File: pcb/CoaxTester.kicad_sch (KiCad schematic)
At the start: 14 parts

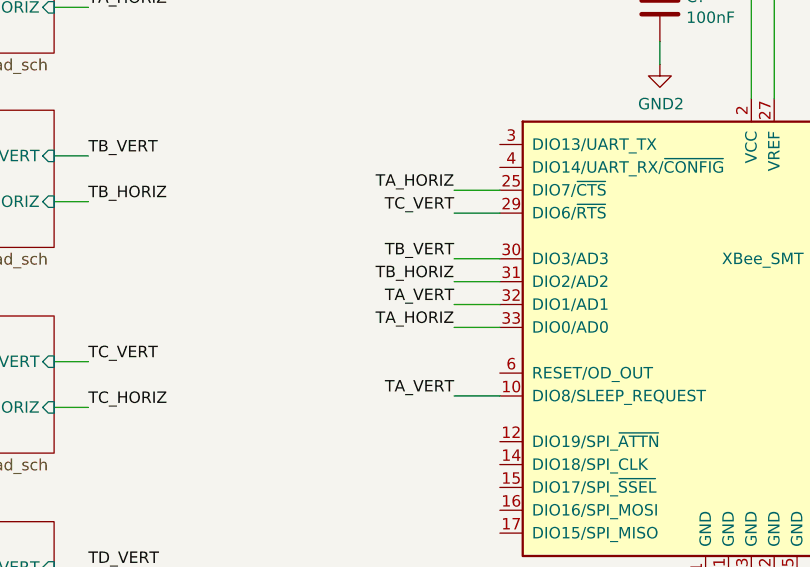
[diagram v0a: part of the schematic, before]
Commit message: Corrections to the coax driver
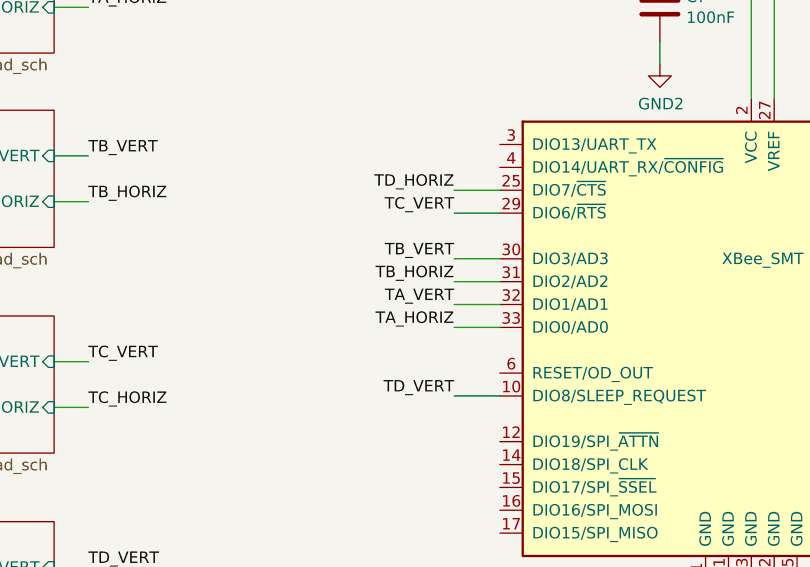
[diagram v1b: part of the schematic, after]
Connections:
- net TA_HORIZ: no longer U?.25 (DIO7/~{CTS})
- net TA_VERT: no longer U?.10 (DIO8/SLEEP_REQUEST)
- net TD_HORIZ: now also U?.25 (DIO7/~{CTS})
- net TD_VERT: now also U?.10 (DIO8/SLEEP_REQUEST)
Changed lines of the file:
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@@
     (effects (font (size 1.27 1.27)) (justify left bottom))
   )
-  (label "TA_HORIZ" (at 325.12 111.76 180)
+  (label "TD_HORIZ" (at 325.12 111.76 180)
     (effects (font (size 1.27 1.27)) (justify right bottom))
   )
@@
     (effects (font (size 1.27 1.27)) (justify right bottom))
   )
-  (label "TA_VERT" (at 325.12 134.62 180)
+  (label "TD_VERT" (at 325.12 134.62 180)
     (effects (font (size 1.27 1.27)) (justify right bottom))
   )

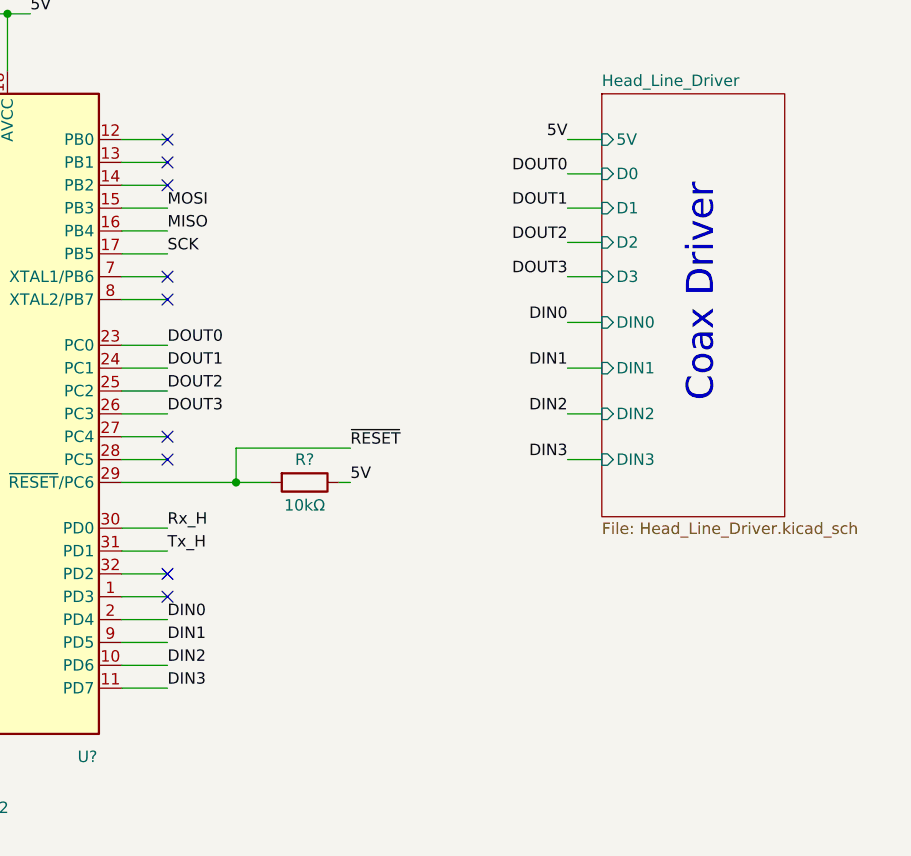
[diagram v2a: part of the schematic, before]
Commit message: Shift register updates - changes the driver from pnp to npn
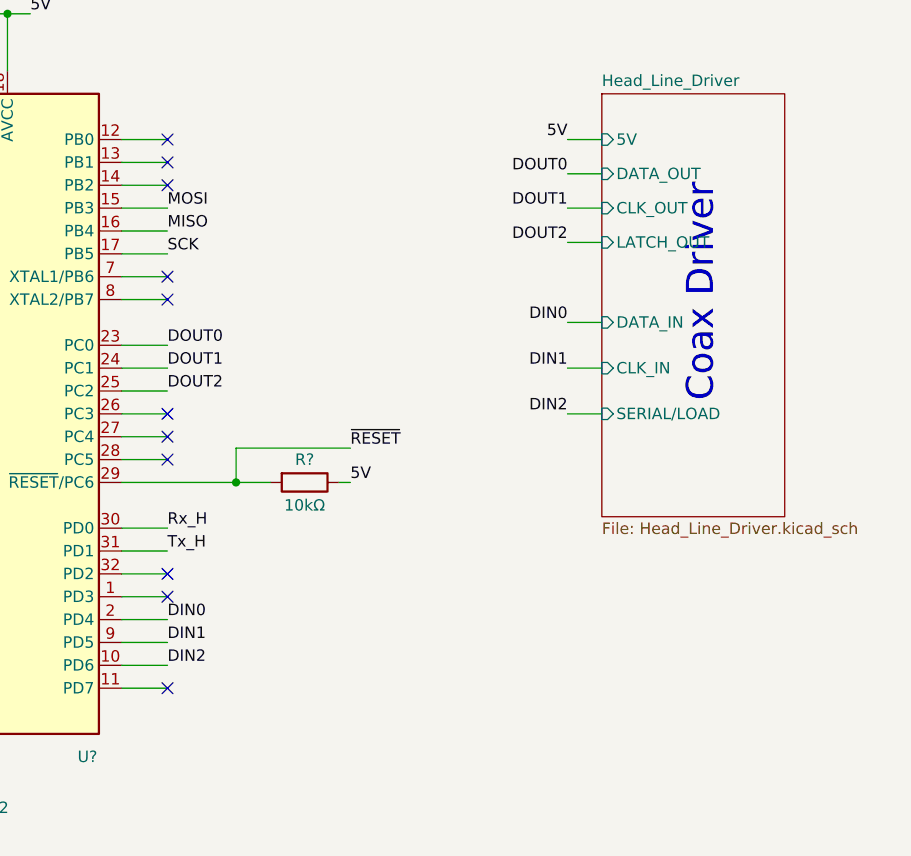
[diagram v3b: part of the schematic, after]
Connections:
- net DIN3: no longer names the net of U?.11 (PD7)
- net DOUT3: no longer names the net of U?.26 (PC3)
- no-connect marks 33 -> 35
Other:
- sheet Head_Line_Driver ports: added CLK_IN, CLK_OUT, DATA_IN, DATA_OUT, LATCH_OUT, SERIAL/LOAD; removed D0, D1, D2, D3, DIN0, DIN1, DIN2, DIN3
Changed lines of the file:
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@@
   (no_connect (at 111.76 116.84))
   (no_connect (at 144.78 234.95))
+  (no_connect (at 111.76 99.06))
+  (no_connect (at 111.76 129.54))
   (no_connect (at 200.66 201.93))
   (no_connect (at 144.78 214.63))
@@
     (stroke (width 0) (type default) (color 0 0 0 0))
   )
-  (wire (pts (xy 160.02 83.82) (xy 156.21 83.82))
-    (stroke (width 0) (type default) (color 0 0 0 0))
-  )
   (wire (pts (xy 177.8 246.38) (xy 177.8 242.57))
     (stroke (width 0) (type default) (color 0 0 0 0))
@@
   )
   (wire (pts (xy 53.34 194.31) (xy 53.34 200.66))
-    (stroke (width 0) (type default) (color 0 0 0 0))
-  )
-  (wire (pts (xy 160.02 104.14) (xy 156.21 104.14))
     (stroke (width 0) (type default) (color 0 0 0 0))
   )
@@
     (effects (font (size 1.27 1.27)) (justify right bottom))
   )
-  (label "DOUT3" (at 111.76 99.06 0)
-    (effects (font (size 1.27 1.27)) (justify left bottom))
-  )
   (label "Rx_L" (at 76.2 246.38 0)
     (effects (font (size 1.27 1.27)) (justify left bottom))
@@
     (effects (font (size 1.27 1.27)) (justify right bottom))
   )
-  (label "DIN3" (at 156.21 104.14 180)
-    (effects (font (size 1.27 1.27)) (justify right bottom))
-  )
   (label "Tx_H" (at 76.2 208.28 0)
     (effects (font (size 1.27 1.27)) (justify left bottom))
@@
     (effects (font (size 1.27 1.27)) (justify left bottom))
   )
-  (label "DIN3" (at 111.76 129.54 0)
-    (effects (font (size 1.27 1.27)) (justify left bottom))
-  )
   (label "DOUT1" (at 111.76 93.98 0)
     (effects (font (size 1.27 1.27)) (justify left bottom))
@@
   (label "DOUT2" (at 111.76 96.52 0)
     (effects (font (size 1.27 1.27)) (justify left bottom))
-  )
-  (label "DOUT3" (at 156.21 83.82 180)
-    (effects (font (size 1.27 1.27)) (justify right bottom))
   )
   (label "~{RESET}" (at 30.48 91.44 0)
@@
       (effects (font (size 1.27 1.27)) (justify left))
     )
-    (pin "D0" input (at 160.02 72.39 180)
-      (effects (font (size 1.27 1.27)) (justify left))
-    )
-    (pin "D1" input (at 160.02 76.2 180)
-      (effects (font (size 1.27 1.27)) (justify left))
-    )
-    (pin "D2" input (at 160.02 80.01 180)
-      (effects (font (size 1.27 1.27)) (justify left))
-    )
-    (pin "D3" input (at 160.02 83.82 180)
-      (effects (font (size 1.27 1.27)) (justify left))
-    )
-    (pin "DIN0" input (at 160.02 88.9 180)
-      (effects (font (size 1.27 1.27)) (justify left))
-    )
-    (pin "DIN1" input (at 160.02 93.98 180)
-      (effects (font (size 1.27 1.27)) (justify left))
-    )
-    (pin "DIN2" input (at 160.02 99.06 180)
-      (effects (font (size 1.27 1.27)) (justify left))
-    )
-    (pin "DIN3" input (at 160.02 104.14 180)
+    (pin "DATA_IN" input (at 160.02 88.9 180)
+      (effects (font (size 1.27 1.27)) (justify left))
+    )
+    (pin "CLK_OUT" input (at 160.02 76.2 180)
+      (effects (font (size 1.27 1.27)) (justify left))
+    )
+    (pin "DATA_OUT" input (at 160.02 72.39 180)
+      (effects (font (size 1.27 1.27)) (justify left))
+    )
+    (pin "LATCH_OUT" input (at 160.02 80.01 180)
+      (effects (font (size 1.27 1.27)) (justify left))
+    )
+    (pin "CLK_IN" input (at 160.02 93.98 180)
+      (effects (font (size 1.27 1.27)) (justify left))
+    )
+    (pin "SERIAL{slash}LOAD" input (at 160.02 99.06 180)
       (effects (font (size 1.27 1.27)) (justify left))
     )
@@
       (reference "#PWR?") (unit 1) (value "GND") (footprint "")
     )
+    (path "/00000000-0000-0000-0000-000061c60b45/488f05c2-7acd-4af4-aa90-1c1495a576e0"
+      (reference "#PWR?") (unit 1) (value "GND") (footprint "")
+    )
+    (path "/00000000-0000-0000-0000-000061c60b45/621f16cc-0225-480e-a2c6-d4d386ae8f5e"
+      (reference "#PWR?") (unit 1) (value "GND") (footprint "")
+    )
     (path "/00000000-0000-0000-0000-000061b6893f/8a323e69-2cf2-41e1-aebc-c2158fec9906"
       (reference "#PWR?") (unit 1) (value "GND2") (footprint "")
     )
+    (path "/00000000-0000-0000-0000-000061c60b45/9bd3b295-cf9b-4409-8a15-32cee0098743"
+      (reference "#PWR?") (unit 1) (value "GND") (footprint "")
+    )
     (path "/00000000-0000-0000-0000-000061c60b45/b1c2b919-2c89-412d-9eb8-2aa456907610"
       (reference "#PWR?") (unit 1) (value "GND") (footprint "")
     )
     (path "/00000000-0000-0000-0000-000061c60b45/b41d50ee-4e44-455a-aa18-b9aaede047cf"
+      (reference "#PWR?") (unit 1) (value "GND") (footprint "")
+    )
+    (path "/00000000-0000-0000-0000-000061c60b45/bb73040e-7ad2-43be-9a70-c0886d63dcb1"
       (reference "#PWR?") (unit 1) (value "GND") (footprint "")
     )
@@
       (reference "J?") (unit 1) (value "Conn_Coaxial") (footprint "CoaxTester:FB_EPG")
     )
+    (path "/00000000-0000-0000-0000-000061c60b45/51220069-eb93-4a0d-9112-dbd4b62d80ad"
+      (reference "J?") (unit 1) (value "CONF1") (footprint "")
+    )
+    (path "/00000000-0000-0000-0000-000061c60b45/88c6a8a5-45d2-424d-bba4-ccab09526957"
+      (reference "J?") (unit 1) (value "CONF2") (footprint "")
+    )
     (path "/00000000-0000-0000-0000-000061b6893f/8e78bb44-6dad-4112-8889-d3094650af50"
       (reference "J?") (unit 1) (value "Conn_Coaxial") (footprint "CoaxTester:FB_EPG")
-    )
-    (path "/00000000-0000-0000-0000-000061c60b45/00000000-0000-0000-0000-000061c64a5c/00000000-0000-0000-0000-000061b4818e"
-      (reference "Q?") (unit 1) (value "BC856BS") (footprint "Package_TO_SOT_SMD:SOT-363_SC-70-6")
-    )
-    (path "/00000000-0000-0000-0000-000061c60b45/00000000-0000-0000-0000-000061c64a57/00000000-0000-0000-0000-000061b5137a"
-      (reference "Q?") (unit 1) (value "BC856BS") (footprint "Package_TO_SOT_SMD:SOT-363_SC-70-6")
-    )
-    (path "/00000000-0000-0000-0000-000061c60b45/00000000-0000-0000-0000-000061c64a42/00000000-0000-0000-0000-000061b7f880"
-      (reference "Q?") (unit 1) (value "BC856BS") (footprint "Package_TO_SOT_SMD:SOT-363_SC-70-6")
-    )
-    (path "/00000000-0000-0000-0000-000061c60b45/00000000-0000-0000-0000-000061c64a49/00000000-0000-0000-0000-000061b88035"
-      (reference "Q?") (unit 1) (value "BC856BS") (footprint "Package_TO_SOT_SMD:SOT-363_SC-70-6")
-    )
-    (path "/00000000-0000-0000-0000-000061c60b45/00000000-0000-0000-0000-000061c64a50/00000000-0000-0000-0000-000061b880d1"
-      (reference "Q?") (unit 1) (value "BC856BS") (footprint "Package_TO_SOT_SMD:SOT-363_SC-70-6")
     )
     (path "/00000000-0000-0000-0000-000061bf30ef"
@@
       (reference "Q?") (unit 1) (value "IRLML2502") (footprint "Micro3")
     )
-    (path "/00000000-0000-0000-0000-000061c60b45/00000000-0000-0000-0000-000061c64a57/00000000-0000-0000-0000-000061b55f9e"
-      (reference "Q?") (unit 2) (value "BC856BS") (footprint "Package_TO_SOT_SMD:SOT-363_SC-70-6")
-    )
-    (path "/00000000-0000-0000-0000-000061c60b45/00000000-0000-0000-0000-000061c64a42/00000000-0000-0000-0000-000061b7f885"
-      (reference "Q?") (unit 2) (value "BC856BS") (footprint "Package_TO_SOT_SMD:SOT-363_SC-70-6")
-    )
-    (path "/00000000-0000-0000-0000-000061c60b45/00000000-0000-0000-0000-000061c64a50/00000000-0000-0000-0000-000061b8803a"
-      (reference "Q?") (unit 2) (value "BC856BS") (footprint "Package_TO_SOT_SMD:SOT-363_SC-70-6")
-    )
-    (path "/00000000-0000-0000-0000-000061c60b45/00000000-0000-0000-0000-000061c64a49/00000000-0000-0000-0000-000061b880d6"
-      (reference "Q?") (unit 2) (value "BC856BS") (footprint "Package_TO_SOT_SMD:SOT-363_SC-70-6")
+    (path "/00000000-0000-0000-0000-000061c60b45/00000000-0000-0000-0000-000061c64a49/2115bce5-b635-450f-85cd-d6c7ceef7506"
+      (reference "Q?") (unit 1) (value "BC847BPN") (footprint "Package_TO_SOT_SMD:SOT-363_SC-70-6")
+    )
+    (path "/00000000-0000-0000-0000-000061c60b45/00000000-0000-0000-0000-000061c64a42/544f0905-f177-4c0c-b536-d1ae7c0db5ae"
+      (reference "Q?") (unit 1) (value "BC847BPN") (footprint "Package_TO_SOT_SMD:SOT-363_SC-70-6")
+    )
+    (path "/00000000-0000-0000-0000-000061c60b45/00000000-0000-0000-0000-000061c64a57/896ec217-3ddf-46ba-b573-cfa104c11bdb"
+      (reference "Q?") (unit 1) (value "BC847BPN") (footprint "Package_TO_SOT_SMD:SOT-363_SC-70-6")
+    )
+    (path "/00000000-0000-0000-0000-000061c60b45/00000000-0000-0000-0000-000061c64a5c/998e620e-4062-4e2d-9f99-12c239685871"
+      (reference "Q?") (unit 1) (value "BC847BPN") (footprint "Package_TO_SOT_SMD:SOT-363_SC-70-6")
+    )
+    (path "/00000000-0000-0000-0000-000061c60b45/00000000-0000-0000-0000-000061c64a50/bac6c401-5aa7-4ff7-8d36-c7d83ee281f6"
+      (reference "Q?") (unit 1) (value "BC847BPN") (footprint "Package_TO_SOT_SMD:SOT-363_SC-70-6")
+    )
+    (path "/00000000-0000-0000-0000-000061c60b45/00000000-0000-0000-0000-000061c64a50/0d7577cc-1a80-4ac4-90b7-bf76e3aa4ffe"
+      (reference "Q?") (unit 2) (value "BC847BPN") (footprint "Package_TO_SOT_SMD:SOT-363_SC-70-6")
+    )
+    (path "/00000000-0000-0000-0000-000061c60b45/00000000-0000-0000-0000-000061c64a57/54dc9a80-5390-4ebf-834d-2edd33b66c5c"
+      (reference "Q?") (unit 2) (value "BC847BPN") (footprint "Package_TO_SOT_SMD:SOT-363_SC-70-6")
+    )
+    (path "/00000000-0000-0000-0000-000061c60b45/00000000-0000-0000-0000-000061c64a49/6c83d8b4-f6df-4eb4-a97e-f267d2f68c82"
+      (reference "Q?") (unit 2) (value "BC847BPN") (footprint "Package_TO_SOT_SMD:SOT-363_SC-70-6")
+    )
+    (path "/00000000-0000-0000-0000-000061c60b45/00000000-0000-0000-0000-000061c64a42/a8be33ce-0e97-4b06-a83d-3d41a1fea3ed"
+      (reference "Q?") (unit 2) (value "BC847BPN") (footprint "Package_TO_SOT_SMD:SOT-363_SC-70-6")
     )
     (path "/00000000-0000-0000-0000-000061c60b45/00000000-0000-0000-0000-000061c64a50/00000000-0000-0000-0000-000061b48177"
@@
       (reference "R?") (unit 1) (value "10kΩ") (footprint "Resistor_SMD:R_0805_2012Metric")
     )
+    (path "/00000000-0000-0000-0000-000061c60b45/43e98e75-6e12-43df-a765-03eed30b44b1"
+      (reference "R?") (unit 1) (value "0Ω") (footprint "")
+    )
     (path "/00000000-0000-0000-0000-000061b6893f/bcc5afab-7526-448b-9943-ad1ddef8e90a"

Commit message: Updates to the shematic for mechanics
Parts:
- added Lg? (x2): KiCad Logo, Symbol:KiCad-Logo2_5mm_SilkScreen, symbol mech:logo
- added Lg? (x2): SJM Logo, mech:MyBasic_rounded_50_1, symbol mech:logo
- added N?: Tail Enclosure, symbol Mechanical:Housing
- added N?: Head Enclosure, symbol Mechanical:Housing
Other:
- note added: "Mechanical"
- note added: "The level shifter is specifically for the XBee module which operates at 3V"
- note added: "XBee Module for the Head device"
- note added: "XBee Module for the Tail device"
- moved on the sheet: C?, J?, U?
